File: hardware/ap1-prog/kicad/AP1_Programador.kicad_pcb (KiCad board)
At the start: 2 copper layers, 52 x 42 mm, 42 parts, among them J1 BASE, J2 USB-C, J3 QWIIC, J4 EXT, SW1 MODO / BOOT, SW2 RESET, U1 ESP32-C3-WROOM-02, U2 AP63203WU, U3 USBLC6-2SC6, U4 TSOP38238

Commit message: AP-1 base a 4 capas, biblioteca JLCPCB y códigos LCSC automáticos
- placa.py: CAPAS=4 con planos internos (In1/In2 GND, tipo power para que
  Freerouting no rutee ahí), vías de costura GND (COSTURA) y zona sin cobre
  bajo la antena en todas las capas.
- AP1_Base: 4 capas JLC04161H-7628 (externas 2 oz, internas 1 oz), 61 vías de
  costura; ERC 0, DRC 0, 0 sin conectar, 0 diferencias.
- tools/jlcpcb.py + jlcpcb_catalogo.csv: 1499 piezas Basic/Preferred de la
  biblioteca JLCPCB-KiCad-Library (CDFER, MIT) y buscador por valor/huella.
- tools/descargar_biblioteca_jlcpcb.sh: instala la biblioteca para KiCad 9 y
  rehace el catálogo.
- salidas.py: BOM con LCSC y clase, RESUMEN_JLCPCB.txt con el cargo de piezas
  Extended, Gerber de todas las capas de cobre, PDF del lado inferior.
- Programador: D1/D2 SS14 -> B5819W (Preferred, misma huella).

Co-Authored-By: Claude Opus 5.5 <noreply@anthropic.com>
Claude-Session: https://claude.ai/code/session_01WVk3oGwfQfGTmAT2PMp8oW
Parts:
- D1, D2: value SS14 -> B5819W
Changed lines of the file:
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@@
 			)
 		)
-		(property "Value" "SS14"
+		(property "Value" "B5819W"
 			(at 0 2.1 0)
 			(layer "F.Fab")
@@
 			)
 		)
-		(property "Value" "SS14"
+		(property "Value" "B5819W"
 			(at 0 2.1 0)
 			(layer "F.Fab")

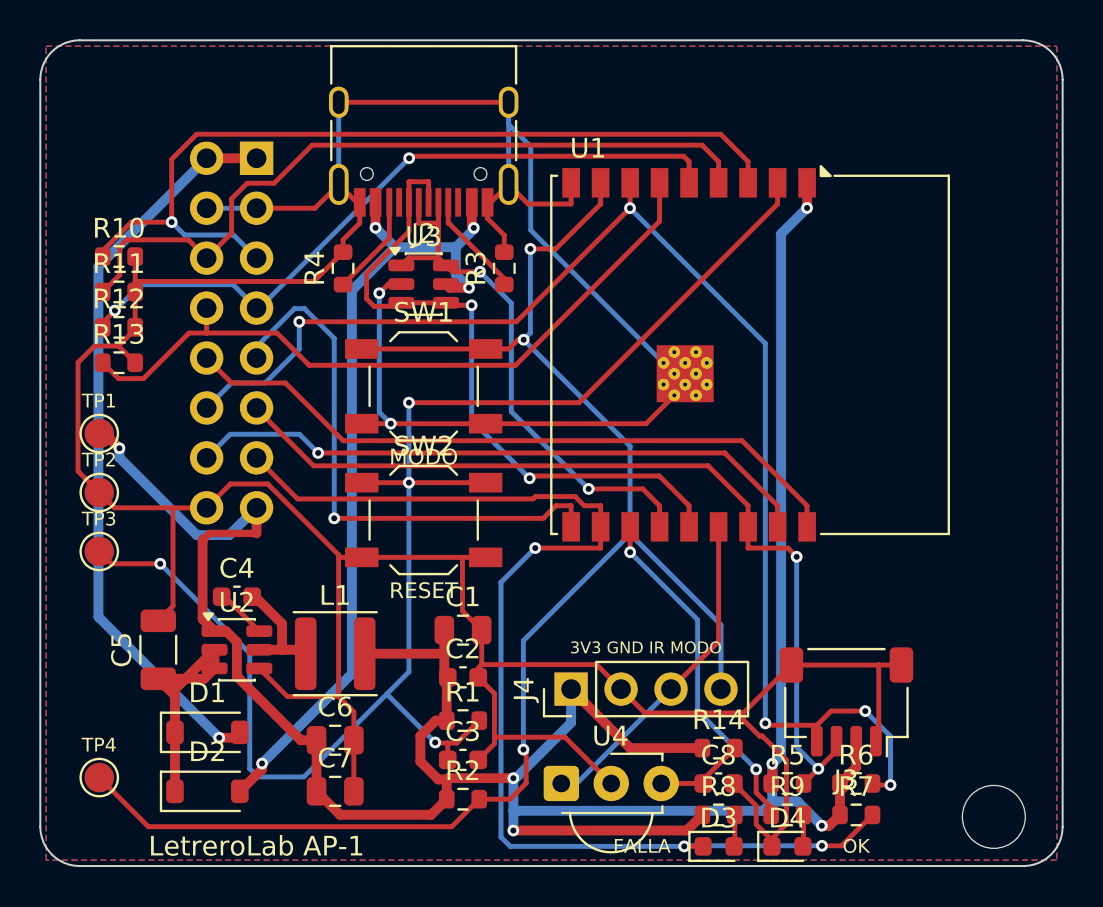
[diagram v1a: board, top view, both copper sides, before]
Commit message: Pedido más económico en JLCPCB: menos piezas Extended y BOM solo SMD
- Base: memoria AT24CS02 -> M24C02 (Preferred). El programa crea el número
  de serie (128 bits al azar con la MAC del programador) si la memoria no trae.
- Programador y AP-0.2: botones TL3342 -> TS-1187A (Basic, misma huella).
  En la AP-0.2 se cambió la huella sin volver a rutear: DRC 0.
- Base: rutas fijas para SWC1/SWC2 y CC2 igual que CC1 (el canal 2 es
  copia del 1, 12.5 mm abajo). Ruteo estable: ERC 0, DRC 0, 0 sin conectar.
- salidas.py: BOM/CPL '_solo_SMD' para soldar a mano clemas y conectores,
  resumen con cargo por código LCSC distinto y costo de piezas Basic.
- jlcpcb.py: piezas reconocidas por huella (botones con valor de etiqueta).
- Cargo de montaje por pedido: base+programador de ~93 a ~84 USD, o ~54 USD
  en el pedido solo SMD.

Co-Authored-By: Claude Opus 5.5 <noreply@anthropic.com>
Claude-Session: https://claude.ai/code/session_01WVk3oGwfQfGTmAT2PMp8oW
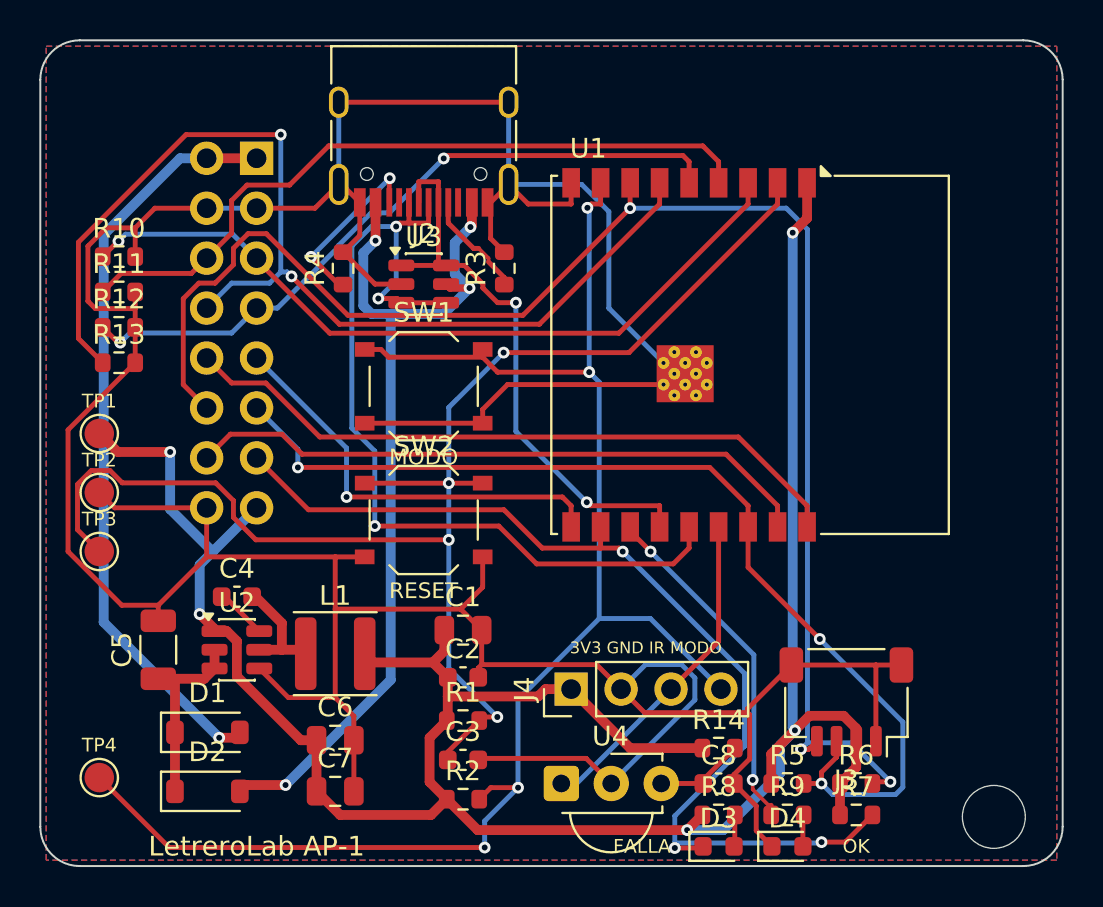
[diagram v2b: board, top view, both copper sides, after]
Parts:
- SW1, SW2: footprint Button_Switch_SMD:SW_SPST_TL3342 -> Button_Switch_SMD:SW_Push_1P1T_XKB_TS-1187A
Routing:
- net /PWM4: track 36.6 -> 54.7 mm, vias 0 -> 2
- net /USB_DP: track 34.4 -> 47.0 mm, vias 2 -> 3
- net /3V3: track 137.7 -> 126.5 mm, vias 6 -> 5
- net /SCL: track 68.4 -> 78.9 mm, vias 5 -> 3
- net /ALERT: track 60.2 -> 52.9 mm
- net /SDA: track 46.0 -> 53.1 mm, vias 2 -> 3
- net /CC1: track 28.5 -> 21.6 mm
- net /PWM1: track 44.2 -> 39.2 mm
- net /VLOG: track 14.5 -> 9.76 mm
- net /GND: track 217.3 -> 221.7 mm, vias 2 -> 0
- net /CC2U: track 5.15 -> 9.11 mm, vias 0 -> 2
- net /EN: track 77.2 -> 73.5 mm
- net /VBUS: track 43.0 -> 46.6 mm
- net /USB_DN: track 27.7 -> 29.5 mm
- net /PWM2: track 38.5 -> 36.8 mm
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
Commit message: Listo para JLCPCB: códigos LCSC, reglas de fabricación y carpeta de pedido
- Códigos LCSC verificados para todas las piezas SMD (INA238, LMR16006,
  UCC27524, AL8860, TMP1075, MOSFET, bobinas, capacitor, fusible, módulo,
  conectores) en tools/jlcpcb.py; piezas reconocidas por huella.
- Shunt: el WSK2512 de 4 terminales se agotó en LCSC; base y AP-0.2 usan un
  HoJLR2512 1 mOhm 2 W (C2924520) con huella propia 'net tie' que conserva
  el sensado Kelvin (tools/huellas/LetreroLab.pretty).
- ESP32-C3-WROOM-02: huella propia con 4 vías de 0.3 mm en lugar de 12 de
  0.2 mm (proceso estándar de JLCPCB). Textos de serigrafía de 0.8 mm o más.
- IND: fusible de 3 A (el mismo de la base).
- AP-0.2 ruteada otra vez con el nuevo shunt.
- Las 4 placas: ERC 0, DRC 0, 0 sin conectar, 0 diferencias y 0 problemas
  con las reglas de fabricación de JLCPCB.
- PEDIDO_JLCPCB/ (+ .zip) con Gerber, BOM y CPL completos o solo SMD por
  placa, y PEDIDO_JLCPCB.md con las opciones exactas del pedido.

Co-Authored-By: Claude Opus 5.5 <noreply@anthropic.com>
Claude-Session: https://claude.ai/code/session_01WVk3oGwfQfGTmAT2PMp8oW
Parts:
- U1: footprint RF_Module:ESP32-C3-WROOM-02 -> LetreroLab:ESP32-C3-WROOM-02_JLC
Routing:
- net /GND: track 221.7 -> 211.3 mm
